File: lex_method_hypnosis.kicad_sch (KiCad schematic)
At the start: 4 parts

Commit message: About to wire up connectors (gulpoid)
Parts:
- added J1, J2: Conn_02x05_Odd_Even, symbol Connector_Generic:Conn_02x05_Odd_Even
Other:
- note added: "female, looking at cable face, pin 1 top left"
- note added: "male, looking at mating face, pin 1 top left"
- moved on the sheet: U2, U3

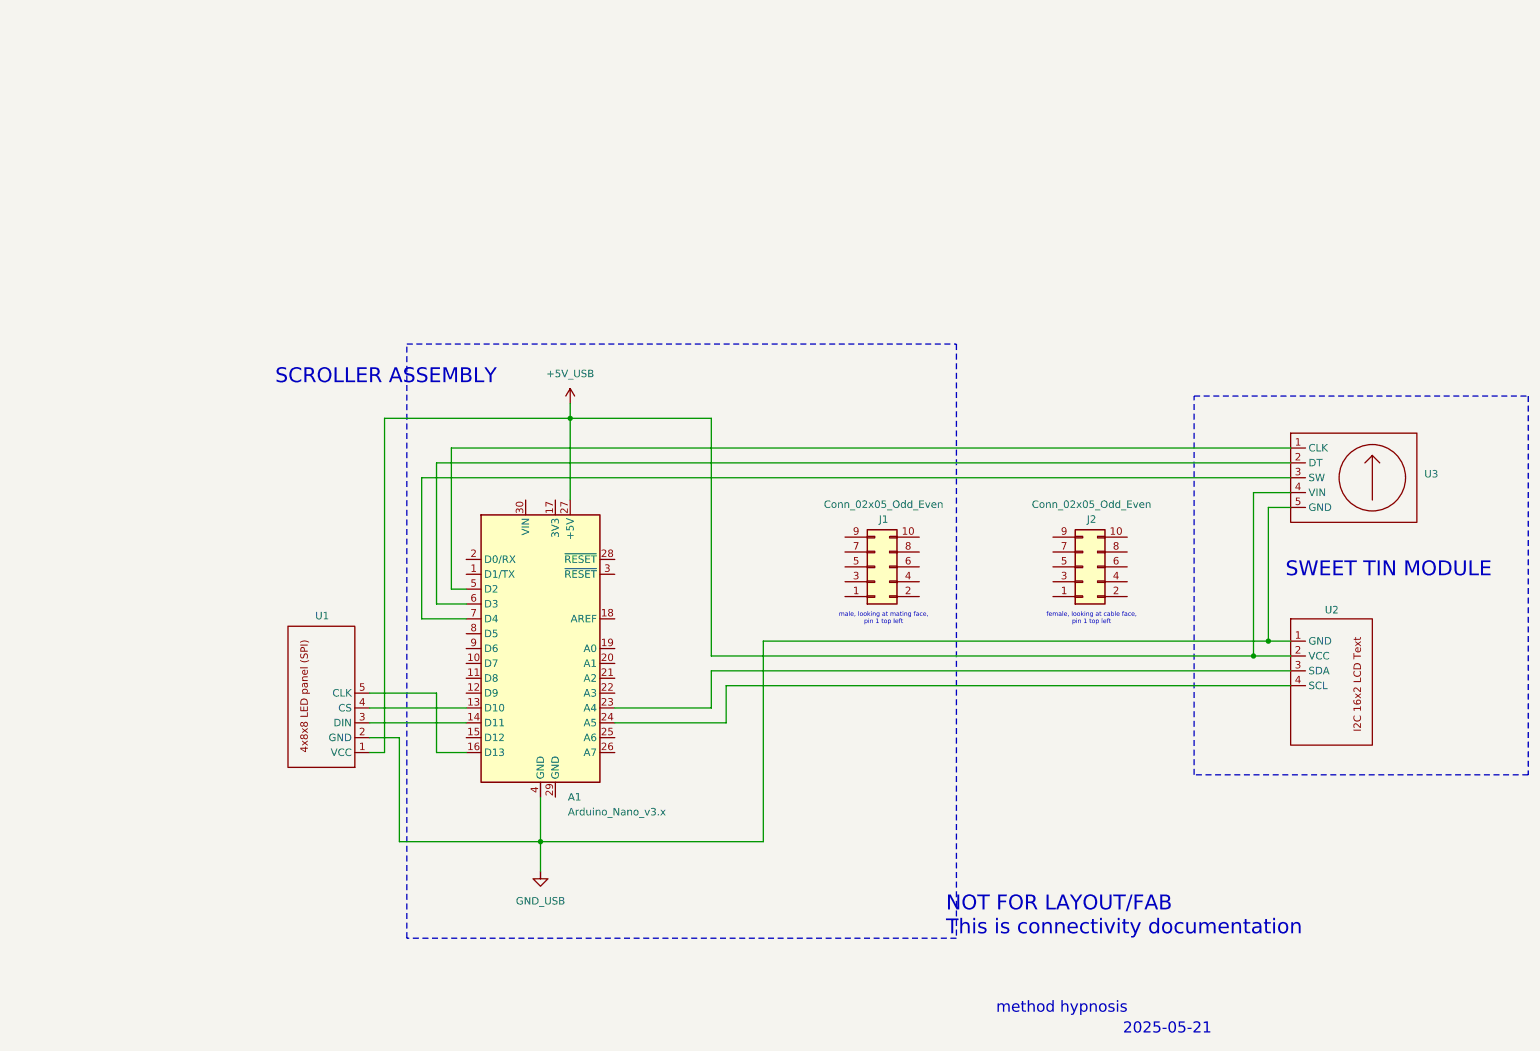
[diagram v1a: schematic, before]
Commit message: Connectors finished (scroller to sweet tin controls)
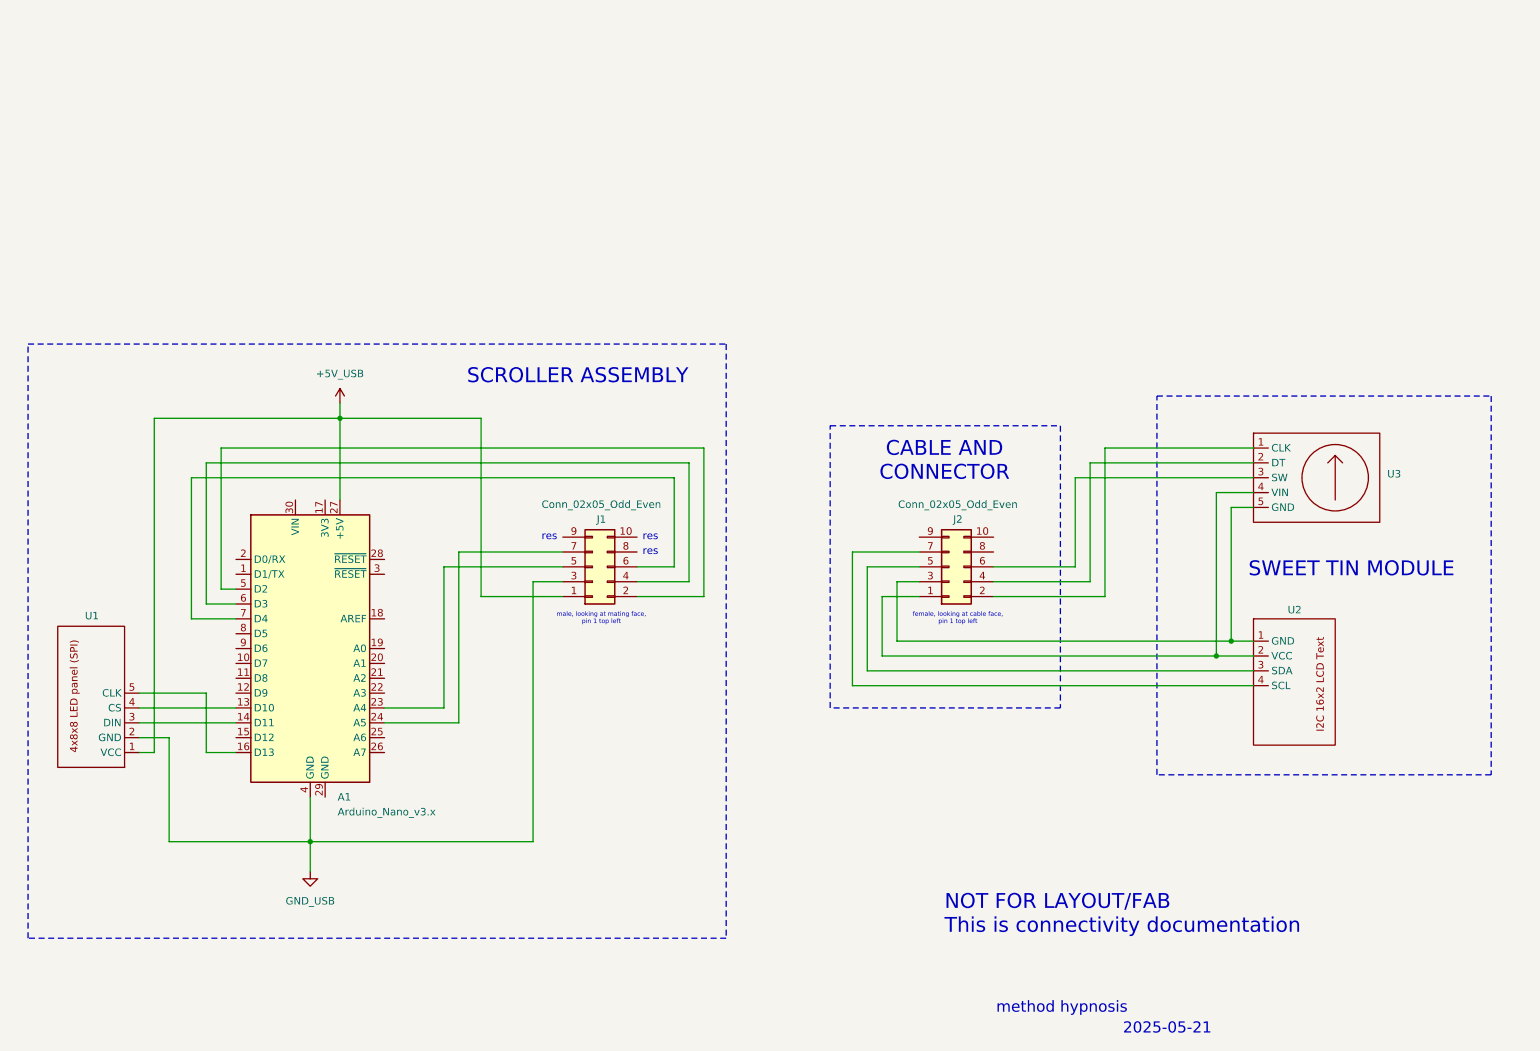
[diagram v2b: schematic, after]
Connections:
- net +5V_USB: now also J1.1 (Pin_1); no longer U2.2 (VCC), U3.4 (VIN)
- net GND_USB: now also J1.3 (Pin_3); no longer U2.1 (GND), U3.5 (GND)
- net at U2.3 (SDA): now also J2.5 (Pin_5); no longer A1.23 (A4)
- net at U2.4 (SCL): now also J2.7 (Pin_7); no longer A1.24 (A5)
- net at A1.5 (D2): now also J1.2 (Pin_2); no longer U3.1 (CLK)
- net at A1.6 (D3): now also J1.4 (Pin_4); no longer U3.2 (DT)
- net at A1.7 (D4): now also J1.6 (Pin_6); no longer U3.3 (SW)
- net at J2.1 (Pin_1): now also U2.2 (VCC), U3.4 (VIN)
- net at J2.2 (Pin_2): now also U3.1 (CLK)
- net at J2.3 (Pin_3): now also U2.1 (GND), U3.5 (GND)
- net at J2.4 (Pin_4): now also U3.2 (DT)
- net at J2.6 (Pin_6): now also U3.3 (SW)
- net at J1.5 (Pin_5): now also A1.23 (A4)
- net at J1.7 (Pin_7): now also A1.24 (A5)
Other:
- note added: "CABLE AND CONNECTOR"
- note added: "res"
- moved on the sheet: A1, J1, J2, U1, U2, U3

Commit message: Add comment to schematic
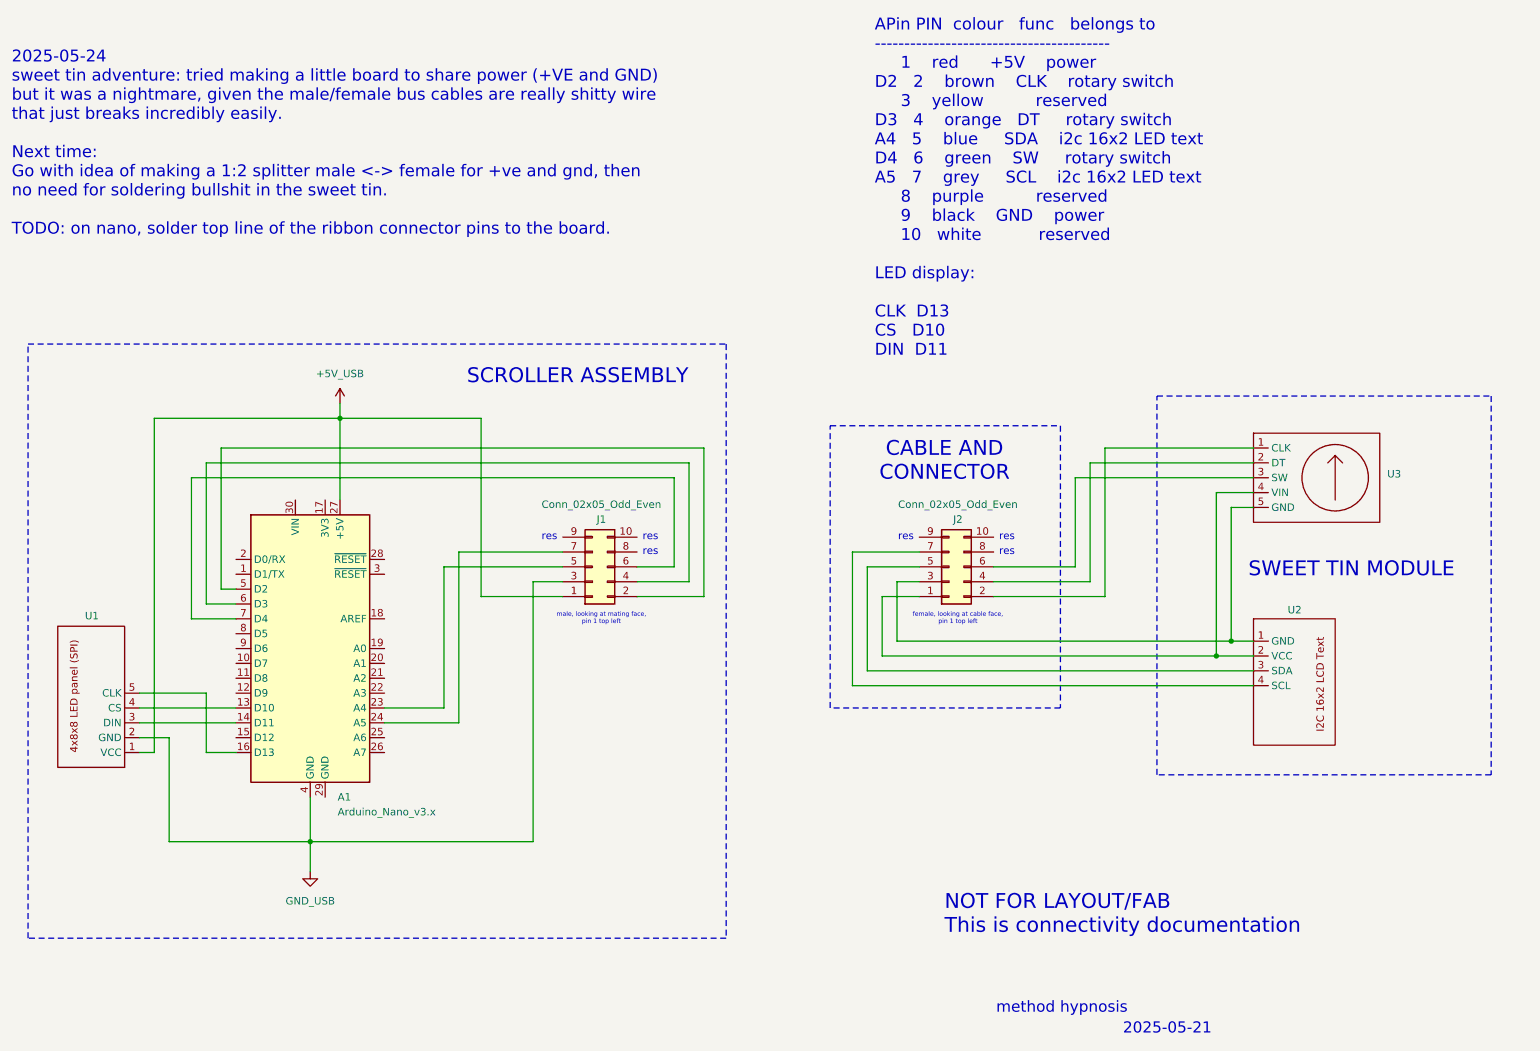
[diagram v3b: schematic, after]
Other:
- note added: "2025-05-24 sweet tin adventure: tried making a little board to share power (+VE and GND) but it was a nightmare, given the male/female bus cables are really shitty wire that just breaks incredibly easily. Next time: Go with idea of making a 1:2 splitter male <-> female for +ve and gnd, then no need for soldering bullshit in the sweet tin. TODO: on nano, solder top line of the ribbon connector pin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"
- note added: "APin PIN colour func belongs to ---------------------------------------- 1 red +5V power D2 2 brown CLK rotary switch 3 yellow reserved D3 4 orange DT rotary switch A4 5 blue SDA i2c 16x2 LED text D4 6 green SW rotary switch A5 7 grey SCL i2c 16x2 LED text 8 purple reserved 9 black GND power 10 white reserved LED display: CLK D13 CS D10 DIN D11"
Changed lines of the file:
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@@
+		)
+	)
+	(text "res"
+		(exclude_from_sim no)
+		(at 191.516 111.76 0)
+		(effects
+			(font
+				(size 1.27 1.27)
+			)
 		)
 	)
@@
 		)
 	)
+	(text "res"
+		(exclude_from_sim no)
+		(at 174.244 109.22 0)
+		(effects
+			(font
+				(size 1.27 1.27)
+			)
+		)
+	)
 	(text "CABLE AND\nCONNECTOR"
 		(exclude_from_sim no)
@@
 		)
 	)
+	(text "res"
+		(exclude_from_sim no)
+		(at 191.516 109.22 0)
+		(effects
+			(font
+				(size 1.27 1.27)
+			)
+		)
+	)
 	(text "SCROLLER ASSEMBLY"
 		(exclude_from_sim no)
@@
 		)
 	)
+	(text "APin PIN  colour   func   belongs to\n----------------------------------------\n     1    red      +5V    power\nD2   2    brown    CLK    rotary switch\n     3    yellow          reserved\nD3   4    orange   DT     rotary switch\nA4   5    blue     SDA    i2c 16x2 LED text\nD4   6    green    SW     rotary switch\nA5   7    grey     SCL    i2c 16x2 LED text\n     8    purple          reserved\n     9    black    GND    power\n     10   white           reserved\n\nLED display:\n\nCLK  D13\nCS   D10\nDIN  D11\n"
+		(exclude_from_sim no)
+		(at 168.91 49.53 0)
+		(effects
+			(font
+				(face "Courier New")
+				(size 2.032 2.032)
+			)
+			(justify left)
+		)
+	)
 	(text "res"
 		(exclude_from_sim no)
@@
 		)
 	)
+	(text "2025-05-24\nsweet tin adventure: tried making a little board to share power (+VE and GND)\nbut it was a nightmare, given the male/female bus cables are really shitty wire\nthat just breaks incredibly easily. \n\nNext time:\nGo with idea of making a 1:2 splitter male <-> female for +ve and gnd, then\nno need for soldering bullshit in the sweet tin.\n\nTODO: on nano, solder top line of the ribbon connector pins to the board.\n"
+		(exclude_from_sim no)
+		(at 21.336 41.91 0)
+		(effects
+			(font
+				(size 2.032 2.032)
+			)
+			(justify left)
+		)
+	)
